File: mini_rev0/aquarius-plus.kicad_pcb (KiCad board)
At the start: 2 copper layers, 128 x 83 mm, 124 parts, among them J1 Power in, J10 FPGA spare, J13 ESP32 spare, J2 ESP USB Host, J3 Audio out, J4 VGA, J9 TF-03A, Q3 2N7002, SW1 SW_DPDT_x2, U1 SN74AHCT1G125DBVR, U10 ESP32-S3-WROOM-1-N4R2, U11 LDL1117S33R, U12 SN74CB3T3245PWR, U13 IS61C5128AS-25QLI, U3 LD1117S12, U4 SN74CB3T3245PWR, U6 XC6SLX9-2TQG144C, U7 Z84C0010AEG, U8 SN74CB3T3245PWR, U9 SN74CB3T3245PWR, X1 SX3M14.31818M20F30TNN

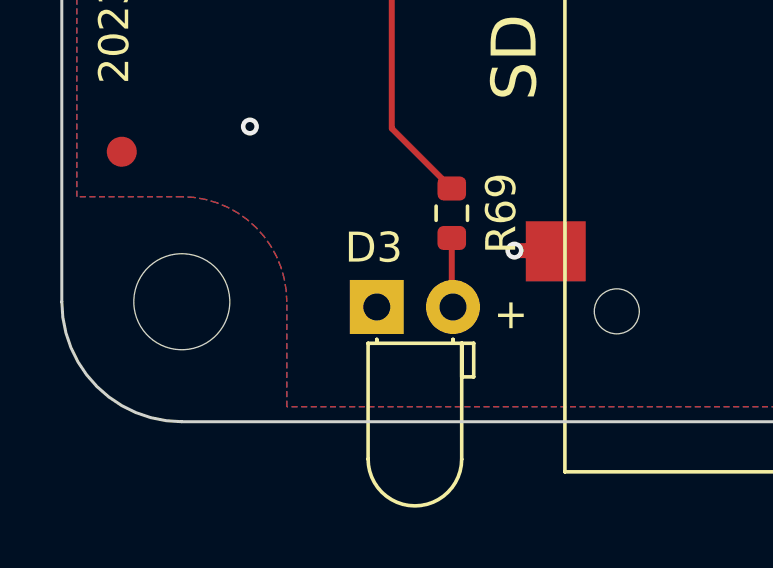
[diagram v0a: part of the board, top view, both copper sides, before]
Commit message: Added - sign to LED footprint.
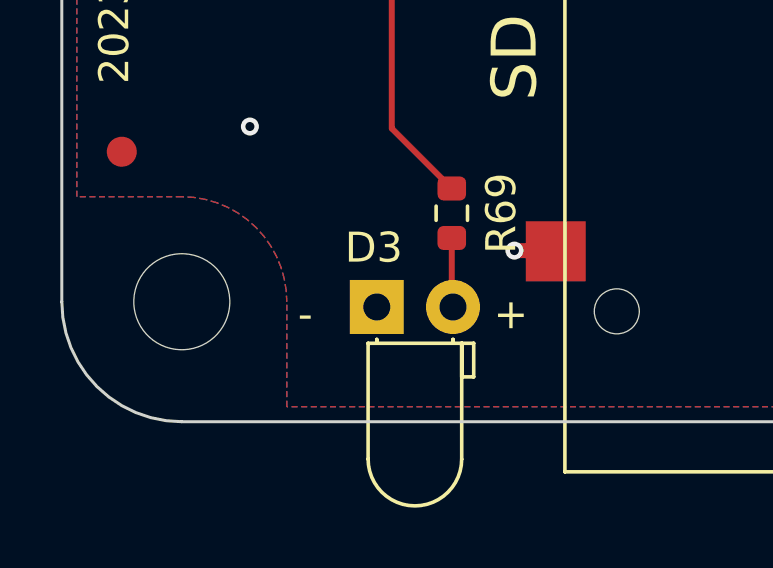
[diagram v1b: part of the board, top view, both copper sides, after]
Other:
- board text added: "-"
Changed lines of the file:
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@@
     (effects (font (size 1.5 1.5) (thickness 0.3)))
+  )
+  (gr_text "-" (at 72.868129 122.427412) (layer "F.SilkS")
+    (effects (font (size 1 1) (thickness 0.15)) (justify left))
   )
   (gr_text "WiFi and Storage" (at 71.5 69.75) (layer "F.SilkS")
